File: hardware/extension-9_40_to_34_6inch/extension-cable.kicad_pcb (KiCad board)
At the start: 2 copper layers, 64.8 x 37 mm, 8 parts, among them J1 XF2M-3315-1A, U1 ED060XC5, U2 ED078KH6, U3 ED060XC5

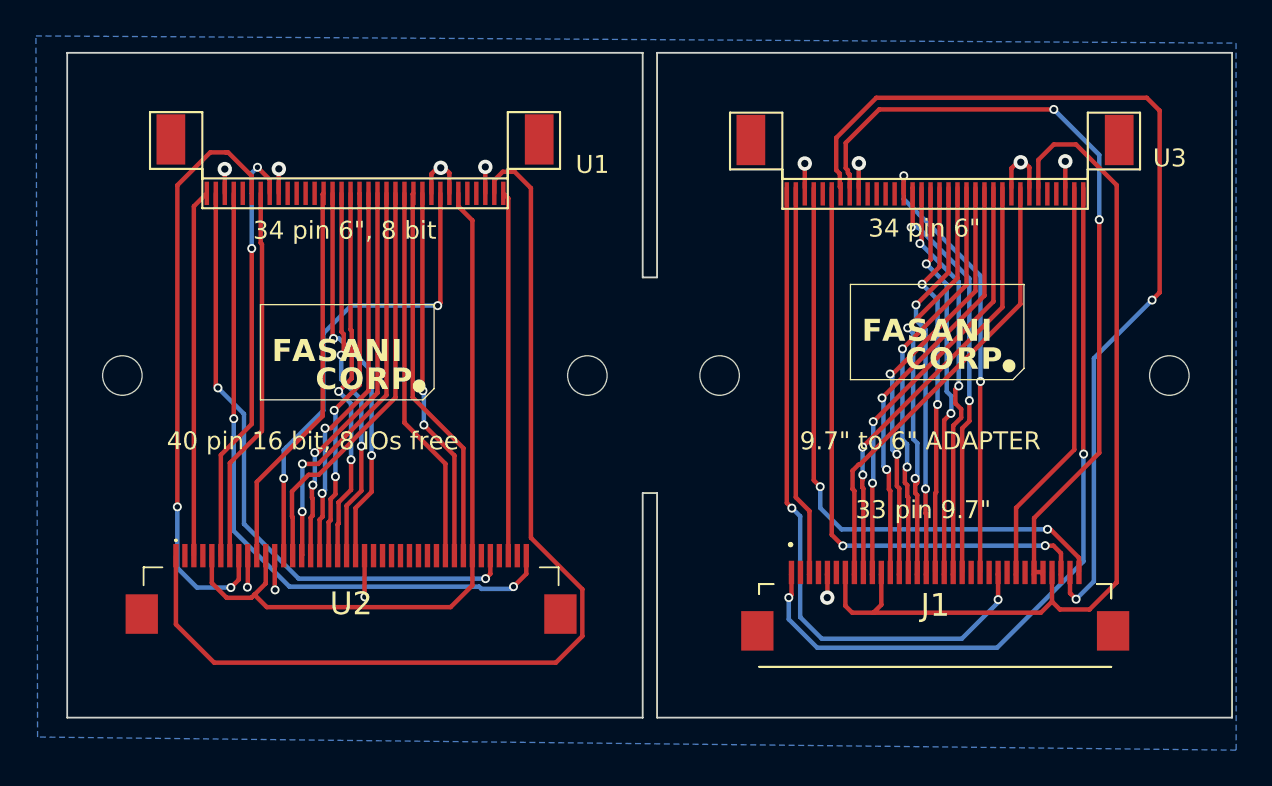
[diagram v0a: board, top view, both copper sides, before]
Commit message: Add PCB tester with LEDs & MicroSD
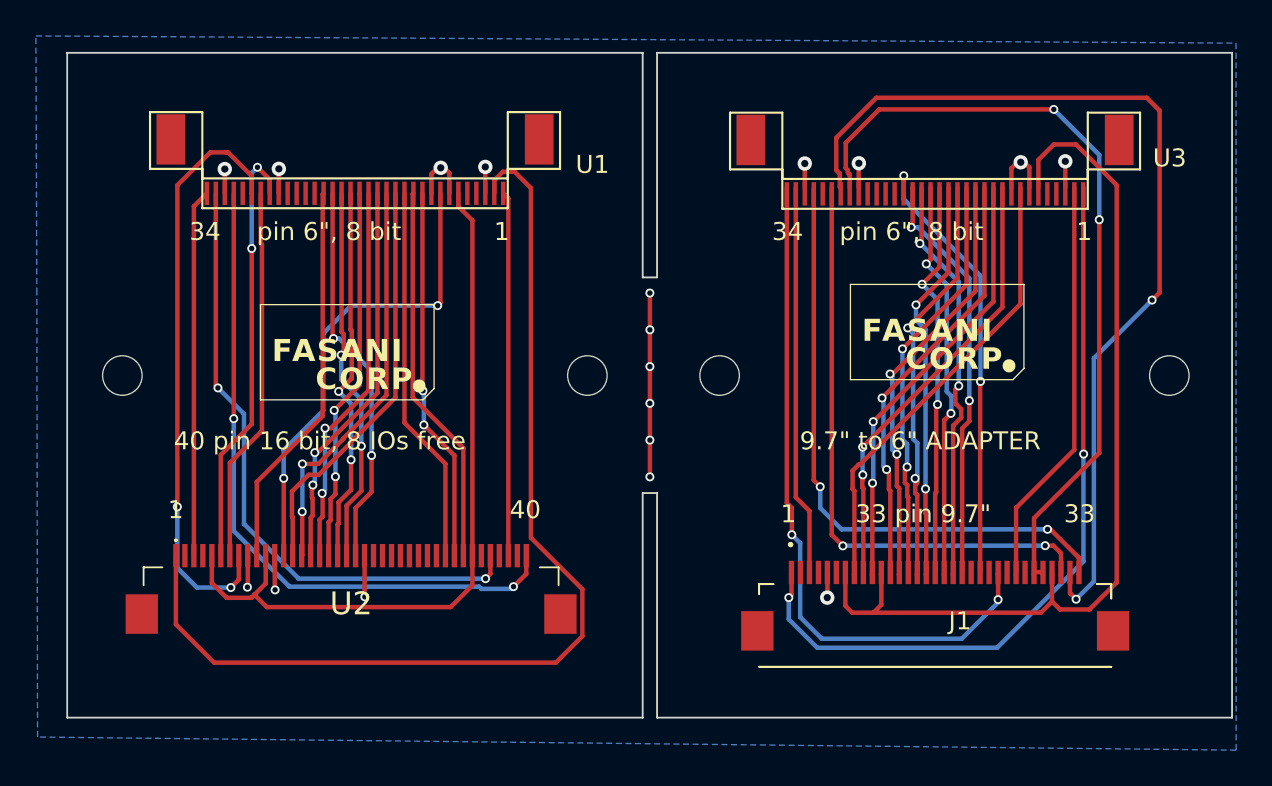
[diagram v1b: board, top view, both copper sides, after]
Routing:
- net GND: track 22.7 -> 32.9 mm, vias 12 -> 18
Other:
- rule pad_to_mask_clearance: 0.051 -> 0
- board text added: "1"
- board text added: "33"
- board text added: "34"
- board text added: "40"
- board text added: "pin 6{dblquote}, 8 bit"
- board text removed: "34 pin 6{dblquote}, 8 bit"
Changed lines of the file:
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@@
   )
   (setup
-    (pad_to_mask_clearance 0.051)
-    (solder_mask_min_width 0.25)
-    (grid_origin 101.83 84.61)
+    (pad_to_mask_clearance 0)
+    (grid_origin 146.11 88.48)
     (pcbplotparams
       (layerselection 0x00010fc_ffffffff)
@@
       (drillshape 0)
       (scaleselection 1)
-      (outputdirectory "gerbers")
+      (outputdirectory "fabrication/")
     )
   )
@@
     (property "ki_description" "ED097OC4 9.7\" epaper display")
     (property "ki_keywords" "epaper eink")
-    (attr smd allow_soldermask_bridges)
-    (fp_text reference "J1" (at 0 -1.125) (layer "F.SilkS")
-        (effects (font (size 1.27 1.27) (thickness 0.254)))
+    (attr smd)
+    (fp_text reference "J1" (at 1.38 -0.25) (layer "F.SilkS")
+        (effects (font (size 1 1) (thickness 0.15)))
     )
     (fp_text value "XF2M-3315-1A" (at 0 -1.125) (layer "F.SilkS") hide
@@
     (property "Sheetname" "")
     (property "ki_description" "ED060XC5 E-Paper screen")
-    (attr smd allow_soldermask_bridges)
+    (attr smd)
     (fp_text reference "U1" (at -13.21 1.6) (layer "F.SilkS")
         (effects (font (size 1 1) (thickness 0.15)))
@@
     (property "Sheetfile" "extension-cable.kicad_sch")
     (property "Sheetname" "")
-    (attr smd allow_soldermask_bridges)
+    (attr smd)
     (fp_text reference "U2" (at 0 0) (layer "F.SilkS")
         (effects (font (size 1.27 1.27) (thickness 0.254)))
@@
     (property "Sheetname" "")
     (property "ki_description" "ED060XC5 E-Paper screen")
-    (attr smd allow_soldermask_bridges)
+    (attr smd)
     (fp_text reference "U3" (at -13.06 1.99) (layer "F.SilkS")
         (effects (font (size 1 1) (thickness 0.15)))
@@
     (effects (font (size 1 1) (thickness 0.15)) (justify left bottom))
   )
-  (gr_text "34 pin 6{dblquote}" (at 122.05 71.85) (layer "F.SilkS")
+  (gr_text "40" (at 102.09 87.52) (layer "F.SilkS")
+    (effects (font (size 1 1) (thickness 0.15)) (justify left bottom))
+  )
+  (gr_text "1" (at 117.17 87.75) (layer "F.SilkS")
+    (effects (font (size 1 1) (thickness 0.15)) (justify left bottom))
+  )
+  (gr_text "1" (at 101.22 72.04) (layer "F.SilkS")
+    (effects (font (size 1 1) (thickness 0.15)) (justify left bottom))
+  )
+  (gr_text "34" (at 84.27 72.04) (layer "F.SilkS")
+    (effects (font (size 1 1) (thickness 0.15)) (justify left bottom))
+  )
+  (gr_text "pin 6{dblquote}, 8 bit" (at 88.03 72.04) (layer "F.SilkS")
+    (effects (font (size 1 1) (thickness 0.15)) (justify left bottom))
+  )
+  (gr_text "33" (at 132.94 87.75) (layer "F.SilkS")
+    (effects (font (size 1 1) (thickness 0.15)) (justify left bottom))
+  )
+  (gr_text "1" (at 133.64 72.04) (layer "F.SilkS")
+    (effects (font (size 1 1) (thickness 0.15)) (justify left bottom))
+  )
+  (gr_text "40 pin 16 bit, 8 IOs free" (at 83.4 83.69) (layer "F.SilkS")
+    (effects (font (size 1 1) (thickness 0.15)) (justify left bottom))
+  )
+  (gr_text "34" (at 116.69 72.04) (layer "F.SilkS")
     (effects (font (size 1 1) (thickness 0.15)) (justify left bottom))
   )
-  (gr_text "34 pin 6{dblquote}, 8 bit" (at 87.81 71.97) (layer "F.SilkS")
+  (gr_text "33 pin 9.7{dblquote}" (at 121.335715 87.75) (layer "F.SilkS")
     (effects (font (size 1 1) (thickness 0.15)) (justify left bottom))
   )
-  (gr_text "40 pin 16 bit, 8 IOs free" (at 83.01 83.69) (layer "F.SilkS")
+  (gr_text "pin 6{dblquote}, 8 bit" (at 120.45 72.04) (layer "F.SilkS")
     (effects (font (size 1 1) (thickness 0.15)) (justify left bottom))
   )
-  (gr_text "33 pin 9.7{dblquote}" (at 121.335715 87.52) (layer "F.SilkS")
+  (gr_text "1" (at 83.07 87.52) (layer "F.SilkS")
     (effects (font (size 1 1) (thickness 0.15)) (justify left bottom))
   )
@@
   (segment (start 119.78 90.4) (end 119.78 91.81) (width 0.25) (layer "F.Cu") (net 5))
   (segment (start 89.24 67.966724) (end 89.249829 67.956895) (width 0.25) (layer "F.Cu") (net 5))
+  (segment (start 109.9 78.962) (end 109.9 81.008) (width 0.25) (layer "F.Cu") (net 5))
   (segment (start 89.02 89.485) (end 89.02 91.37) (width 0.25) (layer "F.Cu") (net 5))
   (segment (start 119.78 91.81) (end 119.77 91.82) (width 0.25) (layer "F.Cu") (net 5))
@@
   (segment (start 97.74 69.32) (end 97.74 68.24) (width 0.25) (layer "F.Cu") (net 5))
   (segment (start 87.52 91.22) (end 87.5 91.24) (width 0.25) (layer "F.Cu") (net 5))
+  (segment (start 109.9 74.87) (end 109.9 76.916) (width 0.25) (layer "F.Cu") (net 5))
   (segment (start 119.751999 90.533097) (end 119.752002 90.5331) (width 0.25) (layer "F.Cu") (net 5))
   (segment (start 94.02 89.485) (end 94.02 91.766052) (width 0.25) (layer "F.Cu") (net 5))
   (segment (start 94.02 91.766052) (end 94.033948 91.78) (width 0.25) (layer "F.Cu") (net 5))
   (segment (start 97.74 68.24) (end 98.08 67.9) (width 0.25) (layer "F.Cu") (net 5))
+  (segment (start 109.9 83.054) (end 109.9 85.1) (width 0.25) (layer "F.Cu") (net 5))
   (segment (start 86.24 69.32) (end 86.24 67.97) (width 0.25) (layer "F.Cu") (net 5))
+  (segment (start 109.9 76.916) (end 109.9 78.962) (width 0.25) (layer "F.Cu") (net 5))
   (segment (start 121.52 67.656724) (end 121.529829 67.646895) (width 0.25) (layer "F.Cu") (net 5))
   (segment (start 89.24 69.32) (end 89.24 67.966724) (width 0.25) (layer "F.Cu") (net 5))
@@
   (segment (start 131.02 67.88) (end 130.73 67.59) (width 0.25) (layer "F.Cu") (net 5))
   (segment (start 98.74 68.19) (end 98.45 67.9) (width 0.25) (layer "F.Cu") (net 5))
+  (segment (start 109.9 81.008) (end 109.9 83.054) (width 0.25) (layer "F.Cu") (net 5))
   (segment (start 133.02 69.01) (end 133.02 67.54) (width 0.25) (layer "F.Cu") (net 5))
   (via (at 119.77 91.82) (size 0.8) (drill 0.4) (layers "F.Cu" "B.Cu") (net 5))
+  (via (at 109.9 76.916) (size 0.5) (drill 0.3) (layers "F.Cu" "B.Cu") (free) (net 5))
   (via (at 118.52 67.66) (size 0.8) (drill 0.4) (layers "F.Cu" "B.Cu") (net 5))
   (via (at 89.249829 67.956895) (size 0.8) (drill 0.4) (layers "F.Cu" "B.Cu") (net 5))
   (via (at 94.033948 91.78) (size 0.5) (drill 0.3) (layers "F.Cu" "B.Cu") (net 5))
+  (via (at 109.9 83.054) (size 0.5) (drill 0.3) (layers "F.Cu" "B.Cu") (free) (net 5))
+  (via (at 109.9 85.1) (size 0.5) (drill 0.3) (layers "F.Cu" "B.Cu") (free) (net 5))
+  (via (at 109.9 78.962) (size 0.5) (drill 0.3) (layers "F.Cu" "B.Cu") (free) (net 5))
   (via (at 133.02 67.54) (size 0.8) (drill 0.4) (layers "F.Cu" "B.Cu") (net 5))
   (via (at 100.74 67.85) (size 0.8) (drill 0.4) (layers "F.Cu" "B.Cu") (net 5))
   (via (at 130.54 67.59) (size 0.8) (drill 0.4) (layers "F.Cu" "B.Cu") (net 5))
   (via (at 89.04 91.39) (size 0.5) (drill 0.3) (layers "F.Cu" "B.Cu") (net 5))
+  (via (at 109.9 81.008) (size 0.5) (drill 0.3) (layers "F.Cu" "B.Cu") (free) (net 5))
+  (via (at 109.9 74.87) (size 0.5) (drill 0.3) (layers "F.Cu" "B.Cu") (free) (net 5))
   (via (at 98.26 67.9) (size 0.8) (drill 0.4) (layers "F.Cu" "B.Cu") (net 5))
   (via (at 121.529829 67.646895) (size 0.8) (drill 0.4) (layers "F.Cu" "B.Cu") (net 5))
@@
   (segment (start 117.63 91.82) (end 117.63 93.03) (width 0.25) (layer "B.Cu") (net 44))
   (segment (start 118.02 86.24) (end 118.78 87) (width 0.25) (layer "F.Cu") (net 46))
-  (segment (start 118.751999 90.533098) (end 118.752001 90.5331) (width 0.25) (layer "F.Cu") (net 46))
   (segment (start 118.02 69.01) (end 118.02 86.24) (width 0.25) (layer "F.Cu") (net 46))
   (segment (start 118.78 87) (end 118.78 90.4) (width 0.25) (layer "F.Cu") (net 46))
@@
   (segment (start 128.3 73.91) (end 124.9 70.51) (width 0.25) (layer "B.Cu") (net 63))
   (segment (start 128.3 79.79) (end 128.3 73.91) (width 0.25) (layer "B.Cu") (net 63))
-  (segment (start 117.8 86.83) (end 117.8 86.84) (width 0.25) (layer "F.Cu") (net 65))
-  (segment (start 117.52 69.01) (end 117.52 86.55) (width 0.25) (layer "F.Cu") (net 65))
+  (segment (start 117.8 86.83) (end 117.52 86.55) (width 0.25) (layer "F.Cu") (net 65))
+  (segment (start 117.52 86.55) (end 117.52 69.01) (width 0.25) (layer "F.Cu") (net 65))
+  (segment (start 117.8 88.32) (end 117.8 86.83) (width 0.25) (layer "F.Cu") (net 65))
   (segment (start 129.251998 90.533097) (end 129.252001 90.5331) (width 0.25) (layer "F.Cu") (net 65))
-  (segment (start 117.52 86.55) (end 117.8 86.83) (width 0.25) (layer "F.Cu") (net 65))
   (segment (start 129.28 90.4) (end 129.28 91.93) (width 0.25) (layer "F.Cu") (net 65))
-  (via (at 117.8 86.84) (size 0.5) (drill 0.3) (layers "F.Cu" "B.Cu") (net 65))
+  (via (at 117.8 88.32) (size 0.5) (drill 0.3) (layers "F.Cu" "B.Cu") (net 65))
   (via (at 129.28 91.93) (size 0.5) (drill 0.3) (layers "F.Cu" "B.Cu") (net 65))
-  (segment (start 117.81 86.84) (end 118.265 87.295) (width 0.25) (layer "B.Cu") (net 65))
+  (segment (start 118.265 92.905) (end 118.265 88.785) (width 0.25) (layer "B.Cu") (net 65))
   (segment (start 118.265 92.905) (end 119.47 94.11) (width 0.25) (layer "B.Cu") (net 65))
+  (segment (start 118.265 88.785) (end 117.8 88.32) (width 0.25) (layer "B.Cu") (net 65))
   (segment (start 129.28 92.09) (end 129.28 91.93) (width 0.25) (layer "B.Cu") (net 65))
-  (segment (start 118.265 87.295) (end 118.265 92.905) (width 0.25) (layer "B.Cu") (net 65))
-  (segment (start 117.8 86.84) (end 117.81 86.84) (width 0.25) (layer "B.Cu") (net 65))
   (segment (start 127.26 94.11) (end 129.28 92.09) (width 0.25) (layer "B.Cu") (net 65))
   (segment (start 119.47 94.11) (end 127.26 94.11) (width 0.25) (layer "B.Cu") (net 65))
